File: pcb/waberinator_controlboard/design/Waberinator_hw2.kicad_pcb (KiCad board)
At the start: 2 copper layers, 57.5 x 99.5 mm, 115 parts, among them J1 Conn_01x04_Pin, J11 Strang A, J12 Strang B, J15 Strang A, J16 Strang B, J17 Conn_01x01_Pin, J18 Conn_01x01_Pin, J19 Conn_01x01_Pin, J20 Conn_01x01_Pin, J21 Conn_01x01_Pin, J22 Conn_01x01_Pin, J23 Conn_01x01_Pin, J4 Conn_01x08_Pin, J7 Strang A, J8 Strang B, Q1 AOSP21321, Q2 SISHA04DN-T1-GE3, Q3 SISHA04DN-T1-GE3, Q4 SISHA04DN-T1-GE3, Q5 SISHA04DN-T1-GE3, Q6 SISHA04DN-T1-GE3, Q7 SISHA04DN-T1-GE3, SW1 SW_SPDT, U1 STM32F030R8Tx, U2 AMS1117-3.3, U3 LM73606QRNPRQ1, U4 LM75B, U5 MCP14A0304xMNY, U6 MCP14A0304xMNY, U7 MCP14A0304xMNY

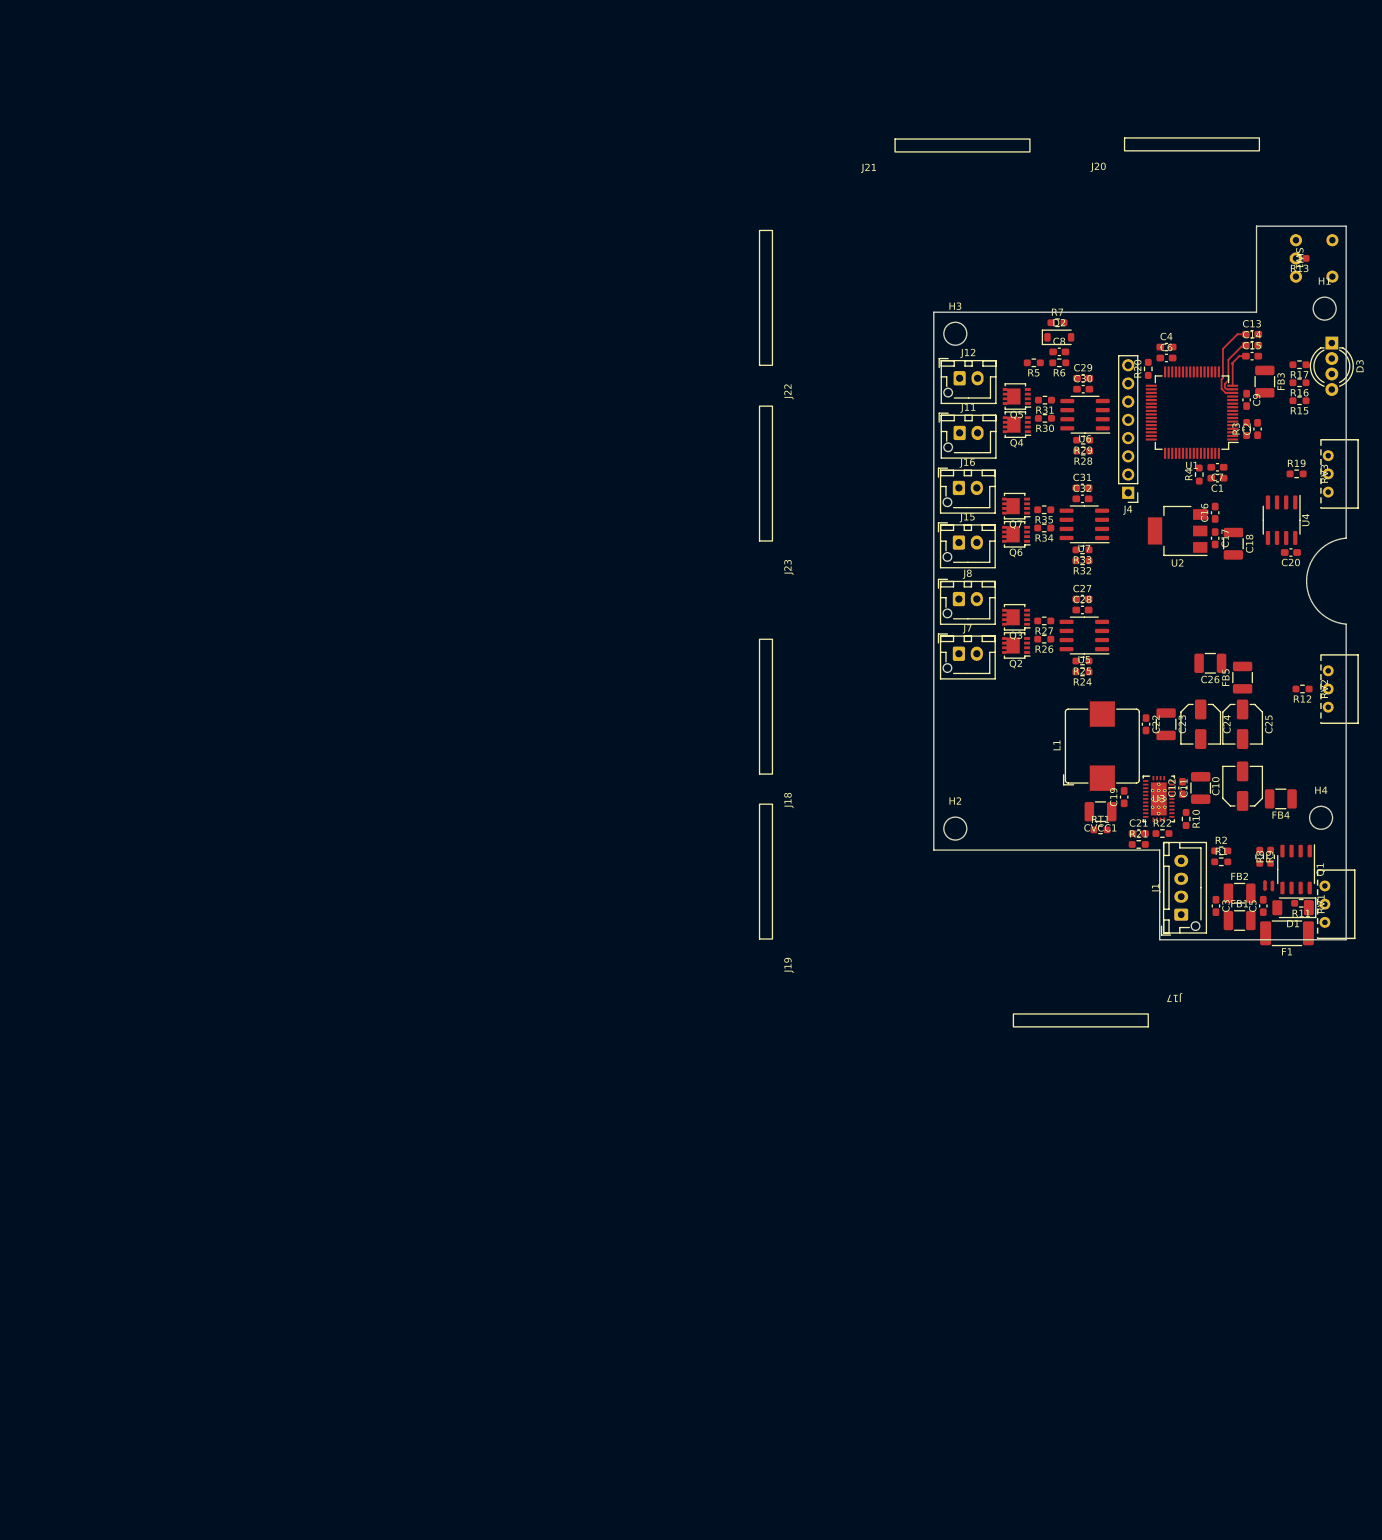
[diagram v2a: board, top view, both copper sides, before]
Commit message: [HW] moved lights connector to top
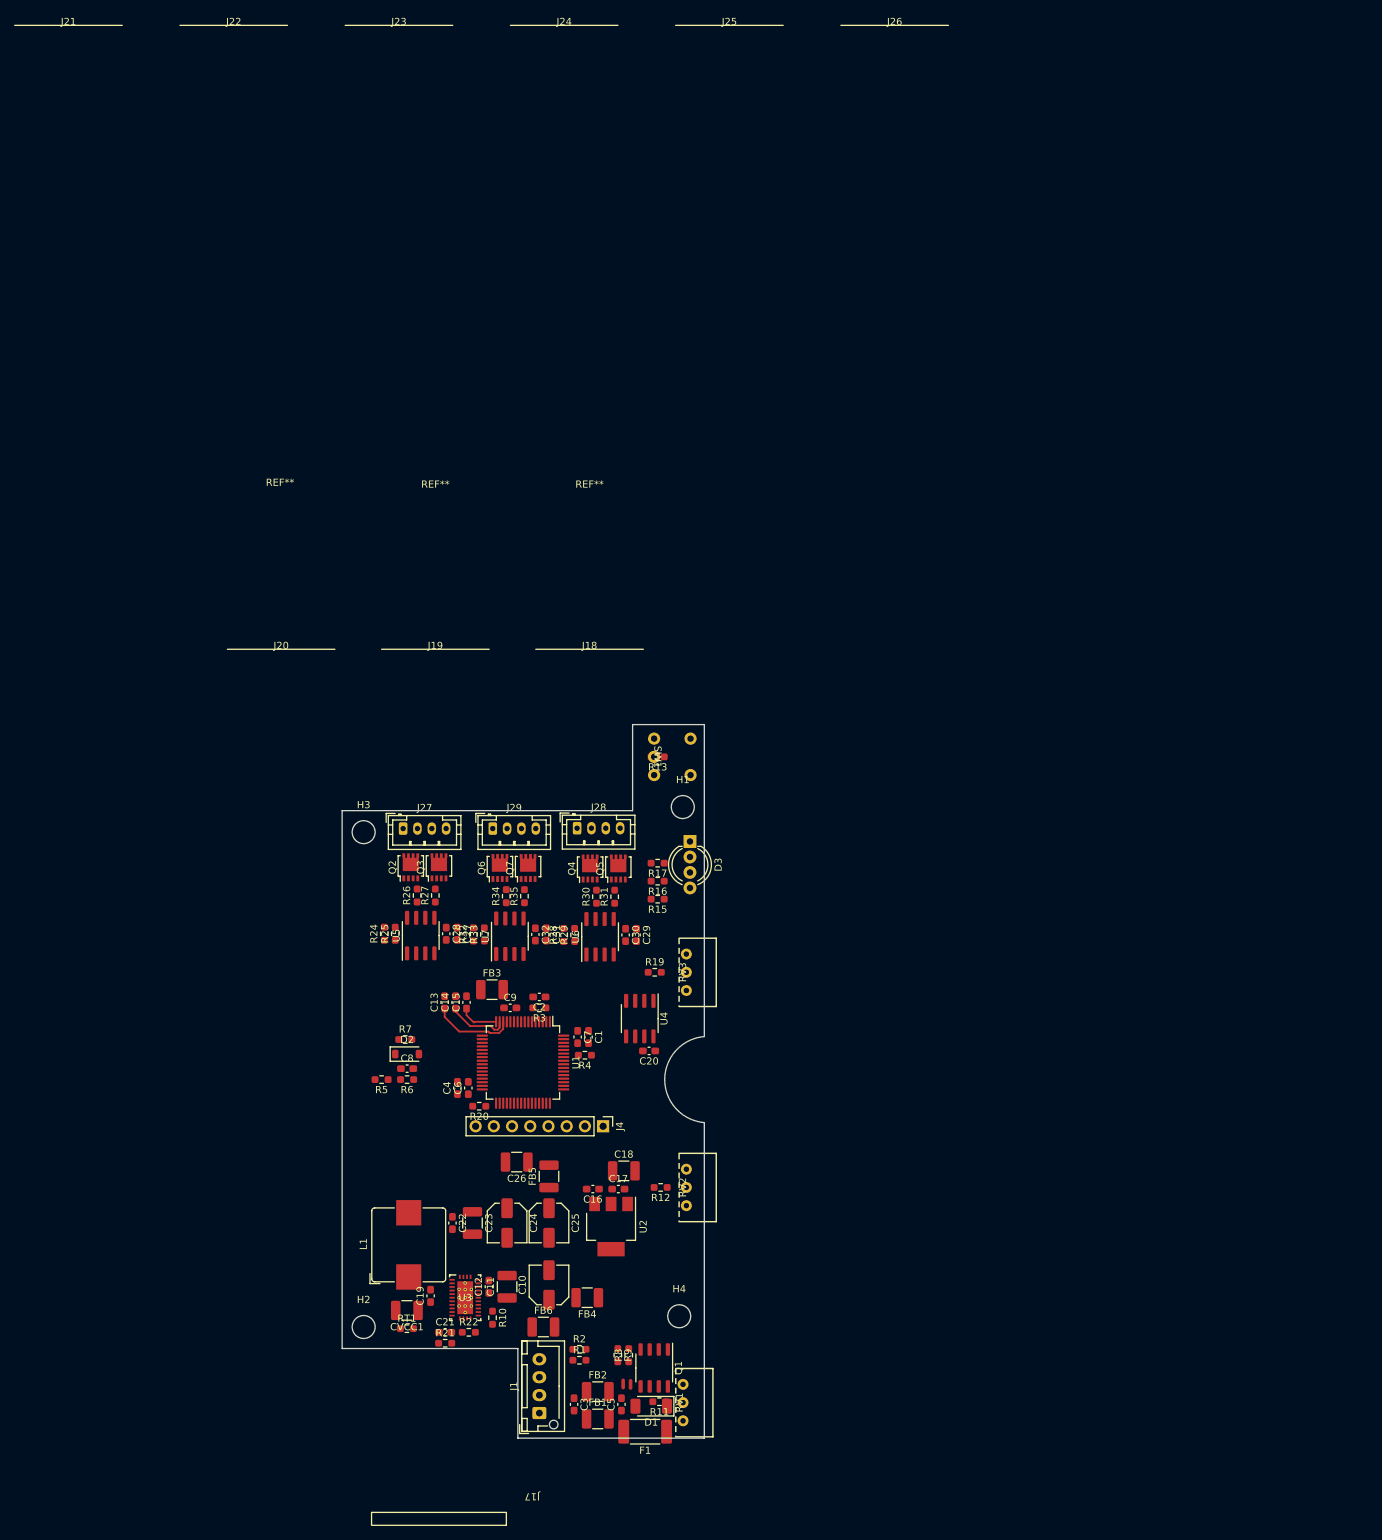
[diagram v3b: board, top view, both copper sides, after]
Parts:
- removed J11, J15, J7: Strang A, Connector_JST:JST_XH_B2B-XH-AM_1x02_P2.50mm_Vertical
- removed J12, J16, J8: Strang B, Connector_JST:JST_XH_B2B-XH-AM_1x02_P2.50mm_Vertical
- added FB6: FerriteBead, Capacitor_SMD:C_1210_3225Metric_Pad1.33x2.70mm_HandSolder, F.Cu at (93.6, 207.0)
- added J24: GX12-4, g7_connectors:gx12_sleeve, F.Cu at (96.5, 25.5)
- added J25: GX12-4, g7_connectors:gx12_sleeve, F.Cu at (119.5, 25.5)
- added J26: GX12-4, g7_connectors:gx12_sleeve, F.Cu at (142.5, 25.5)
- added J27: Conn_01x04, Connector_JST:JST_PH_B4B-PH-K_1x04_P2.00mm_Vertical, F.Cu at (74.0, 137.5)
- added J28: Conn_01x04, Connector_JST:JST_PH_B4B-PH-K_1x04_P2.00mm_Vertical, F.Cu at (98.3, 137.4)
- added J29: Conn_01x04, Connector_JST:JST_PH_B4B-PH-K_1x04_P2.00mm_Vertical, F.Cu at (86.5, 137.5)
- added REF**: gx12_plug, g7_connectors:gx12_plug, F.Cu at (78.5, 90.0)
- added REF**: gx12_plug, g7_connectors:gx12_plug, F.Cu at (100.0, 90.0)
- added REF**: gx12_plug, g7_connectors:gx12_plug, F.Cu at (56.8, 89.8)
- J17: value Conn_01x01_Pin -> GX16-4
- J18, J19, J20, J21, J22, J23: value Conn_01x01_Pin -> GX12-4; footprint g7_connectors:Chassis_Connector -> g7_connectors:gx12_sleeve
- moved C13 146.1 mm to (79.8, 161.7), turned to 90 degrees
- moved J20 144.8 mm to (57.0, 112.5)
- moved C14 144.0 mm to (81.3, 161.7), turned to 90 degrees
- moved C4 143.0 mm to (81.6, 173.7), turned to 90 degrees
- moved C15 141.8 mm to (82.8, 161.7), turned to 90 degrees
- moved C6 140.9 mm to (83.1, 173.7), turned to 90 degrees
- moved R20 138.8 mm to (84.6, 176.2), turned to 180 degrees
- moved FB3 137.1 mm to (86.4, 160.0), turned to 0 degrees
- moved C8 135.1 mm to (74.6, 171.0)
- moved D2 135.1 mm to (74.6, 168.9)
- moved R5 135.1 mm to (71.0, 172.5)
- moved R6 135.1 mm to (74.6, 172.5)
- moved R7 135.1 mm to (74.3, 166.9)
- moved C9 133.2 mm to (88.9, 162.5), turned to 0 degrees
- moved U1 130.1 mm to (90.7, 170.1), turned to -90 degrees
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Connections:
- J1 pad 3: Net-(J1-Pin_3) -> /bat_kelvin+
- J1 pad 4: Net-(J1-Pin_4) -> /bat_kelvin-
- NT1 pad 1: Net-(NT1-Pad1) -> unconnected-(NT1-Pad1)
- R5 pad 2: Net-(NT1-Pad1) -> /bat_kelvin+
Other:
- board size 57.5 x 99.5 mm -> 50.5 x 99.5 mm
- board text added: "Equally Spread across x-Axis"

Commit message: [HW] Details
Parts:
- R24, R25, R28, R29, R32, R33: footprint Resistor_SMD:R_0603_1608Metric_Pad0.98x0.95mm_HandSolder -> Resistor_SMD:R_0402_1005Metric_Pad0.72x0.64mm_HandSolder
- moved R25 5.61 mm to (78.5, 152.5)
- moved R33 5.42 mm to (90.8, 152.5)
- moved R29 5.34 mm to (103.2, 152.5)
- moved R32 4.45 mm to (88.2, 152.5)
- moved R24 4.38 mm to (75.8, 152.5)
- moved R28 4.37 mm to (100.8, 152.5)

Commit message: finalize BOL
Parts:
- moved H2 84.3 mm to (111.5, 134.5)
- moved H3 69.9 mm to (90.0, 204.5)
- moved C8 48.6 mm to (112.0, 202.0)
- moved D2 48.6 mm to (112.0, 200.0)
- moved R5 48.6 mm to (108.4, 203.5)
- moved R6 48.6 mm to (112.0, 203.5)
- moved R7 48.6 mm to (111.7, 197.9)
- moved H4 48.1 mm to (69.5, 184.0)
- moved H1 44.2 mm to (69.5, 142.5)
- moved C13 36.1 mm to (110.4, 180.9), turned to -90 degrees
- moved U4 35.8 mm to (76.0, 182.0), turned to 0 degrees
- moved C14 33.6 mm to (108.9, 180.9), turned to -90 degrees
- moved C15 31.1 mm to (107.4, 180.9), turned to -90 degrees
- moved C20 30.3 mm to (80.5, 180.7), turned to -90 degrees
- moved FB3 28.6 mm to (103.8, 182.7), turned to 180 degrees
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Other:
- board size 50.5 x 99.5 mm -> 49.5 x 104 mm

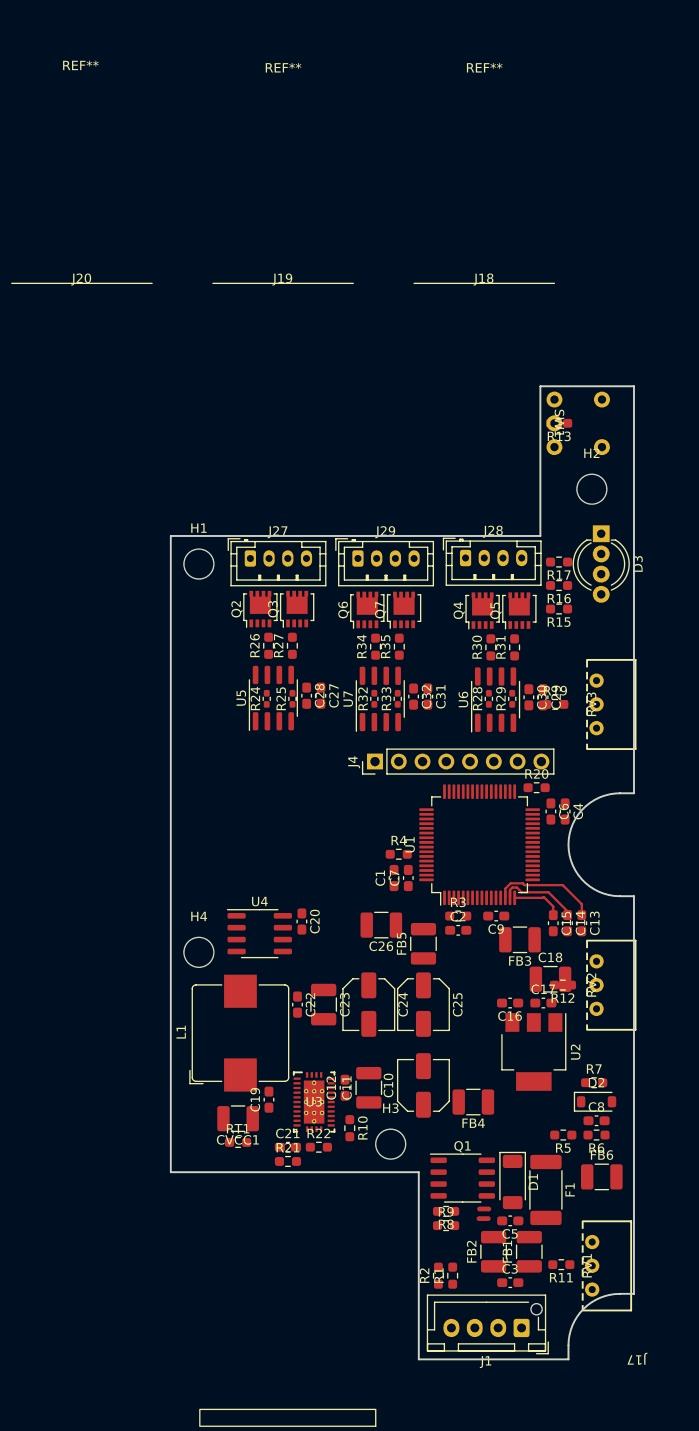
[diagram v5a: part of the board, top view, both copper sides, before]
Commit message: [HW] pcb production ready
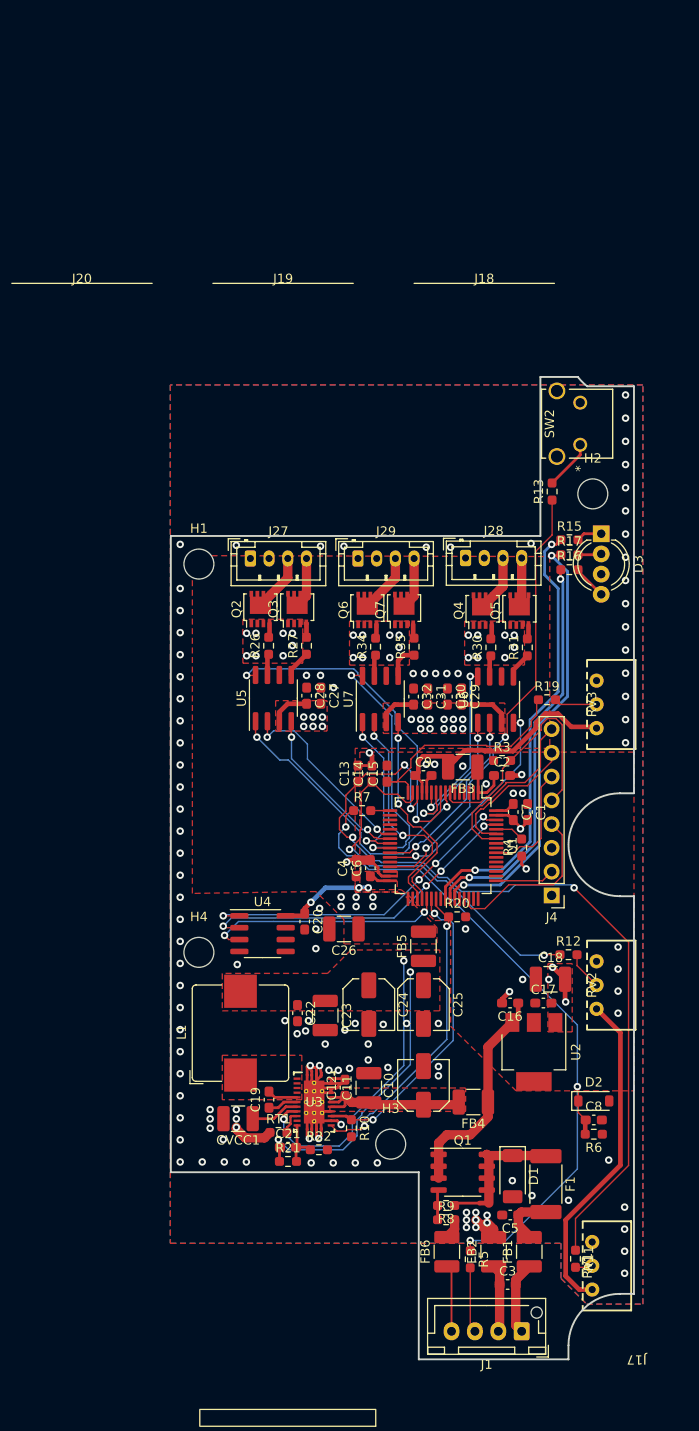
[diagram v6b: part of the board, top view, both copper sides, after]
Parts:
- removed NT1: NetTie_2, NetTie:NetTie-2_SMD_Pad0.5mm
- removed R1, R2: 100, Resistor_SMD:R_0603_1608Metric_Pad0.98x0.95mm_HandSolder
- removed R24, R25, R28, R29, R32, R33: 1, Resistor_SMD:R_0402_1005Metric_Pad0.72x0.64mm_HandSolder
- removed REF** (x3): gx12_plug, g7_connectors:gx12_plug
- removed SW1: SW_SPDT, g7_hmi:switch_800usp8p1a1m6re
- added SW2: sw_te_1-1825027-1, g7_hmi:sw_te_1-1825027-1, F.Cu at (110.3, 129.8)
- moved R7 38.2 mm to (87.0, 168.8)
- moved C13 28.8 mm to (86.5, 164.9), turned to 90 degrees
- moved C14 26.3 mm to (88.0, 164.9), turned to 90 degrees
- moved C15 23.9 mm to (89.6, 164.9), turned to 90 degrees
- moved J4 23.7 mm to (107.2, 177.9), turned to 180 degrees
- moved C4 23.2 mm to (86.3, 175.0), turned to 90 degrees
- moved C6 20.2 mm to (87.8, 175.0), turned to 90 degrees
- moved FB3 19.4 mm to (97.7, 164.2)
- moved FB6 18.4 mm to (96.0, 216.0), turned to 90 degrees
- moved R3 17.3 mm to (101.9, 163.5)
- moved C2 17.2 mm to (101.9, 165.1)
- moved C9 16.9 mm to (93.5, 165.1), turned to 0 degrees
- moved R5 16.6 mm to (98.5, 216.8), turned to -90 degrees
- moved R20 16.2 mm to (97.1, 180.2)
- moved C1 15.9 mm to (104.6, 169.0), turned to -90 degrees
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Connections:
- U3 pad V: (no net) -> RET
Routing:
- net +3.3VA: track 0.00 -> 106.3 mm
- net RET: track 0.00 -> 88.7 mm, vias 0 -> 160
- net /adc_brightness: track 11.5 -> 90.6 mm, vias 0 -> 4
- net Net-(D2-K): track 0.00 -> 74.4 mm, vias 0 -> 3
- net /lm76606_out: track 0.00 -> 64.8 mm, vias 0 -> 5
- net /button1: track 0.00 -> 48.0 mm, vias 0 -> 2
- net /tim1_ch1_indicator_led1: track 0.00 -> 47.5 mm, vias 0 -> 2
- net /tim1_ch3_indicator_led3: track 0.00 -> 45.9 mm, vias 0 -> 2
- net /tim1_ch2_indicator_led2: track 0.00 -> 42.8 mm, vias 0 -> 2
- net /ledstring2_drv_en: track 0.00 -> 36.9 mm, vias 0 -> 2
- net /i2c1_scl: track 0.00 -> 35.6 mm, vias 0 -> 4
- net /i2c1_sda: track 0.00 -> 35.4 mm, vias 0 -> 4
- net /lm73606_en: track 0.00 -> 33.4 mm, vias 0 -> 2
- net /adc_frequency: track 8.56 -> 41.6 mm, vias 0 -> 2
- net /lm73606_pg: track 0.00 -> 32.9 mm, vias 0 -> 2
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- added copper zone on F.Cu, net +3V3
- added copper zone on In2.Cu, net +3V3
- added copper zone on F.Cu, net /VLed
- added copper zone on In2.Cu, net /VLed
- added copper zone on F.Cu, net /lm76606_out
- added copper zone on F.Cu, net /lm_sw
- added copper zone on F.Cu, net /lm_vin
- added copper zone on B.Cu, net RET
- added copper zone on F.Cu, net RET
- added copper zone on In1.Cu, net RET
- added copper zone on In2.Cu, net RET
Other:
- board size 49.5 x 104 mm -> 49.5 x 105 mm
- copper layers 2 -> 4

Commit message: [HW] finish layout
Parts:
- moved R7 0.25 mm to (87.2, 168.8)
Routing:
- net /tim1_ch1_indicator_led1: track 47.5 -> 46.3 mm
- net /adc_brightness: track 90.6 -> 89.5 mm
- net /ledstring1_drv_en: track 32.0 -> 32.7 mm
- net RET: vias 160 -> 174
- net /VLed: vias 14 -> 20
- net +3V3: vias 10 -> 18
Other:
- board text added: "Waberinator Controlboard V2.0"

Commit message: [HW] misc adjustments to mechanics
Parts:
- removed J17: GX16-4, g7_connectors:Chassis_Connector
- removed J18, J19, J20, J21, J22, J23, J24, J25, J26: GX12-4, g7_connectors:gx12_sleeve
- added D4: SD103CW-E3-08, Diode_SMD:D_SOD-123, F.Cu at (100.0, 219.3)
- moved R13 6.25 mm to (113.5, 135.0)
- moved SW2 3.30 mm to (113.4, 130.8)
- moved H2 2.62 mm to (109.1, 135.8)
- moved C3 1.70 mm to (104.2, 219.5)
- moved RV1 1.28 mm to (112.8, 217.5)
- moved RV2 0.82 mm to (112.8, 187.5)
- moved RV3 0.82 mm to (112.8, 157.5)
- moved FB2 0.50 mm to (101.3, 215.6)
- moved FB1 0.50 mm to (104.8, 215.5)
- moved R5 0.45 mm to (98.7, 216.4)
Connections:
- R5 pad 2: /bat_kelvin+ -> Net-(D4-K)
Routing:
- net Net-(D4-K): track 0.00 -> 3.84 mm
- net /button1: track 48.0 -> 50.8 mm
- net Net-(R13-Pad2): track 5.33 -> 3.38 mm
- net /DC_IN-: track 7.26 -> 9.05 mm
- net /bat_kelvin+: track 6.99 -> 5.47 mm
- net Net-(R11-Pad2): track 1.85 -> 3.14 mm
- net /lm76606_out: track 64.8 -> 65.7 mm
- net +3.3VA: track 106.3 -> 107.3 mm
- net Net-(R19-Pad2): track 4.59 -> 5.41 mm
- net Net-(D2-K): track 74.3 -> 74.8 mm
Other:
- board size 49.5 x 105 mm -> 49.5 x 104 mm
